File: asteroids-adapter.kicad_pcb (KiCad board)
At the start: 2 copper layers, 88 x 90.2 mm, 15 parts, among them J1 Asteroids PCB connector, J2 Asteroids harness connector, U1 TL074

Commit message: Fixed DC-DC footprint and silk screen info
- Downloaded from CUI website

- fixed connector labels
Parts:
- VR1: value CUI PESE1-S5-D15-M 5V to +/-15V DC-DC converter 34 mA -> CUI PESE1-S5-D15-M; footprint asteroids-adapter:CUI PESE1 DC-DC dual out -> asteroids-adapter:CONV_PESE1-S5-D15-M
- moved C1 2.19 mm to (170.5, 99.8)
- moved VR1 1.32 mm to (167.8, 108.3), turned to 90 degrees
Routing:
- net +15V: track 35.4 -> 37.5 mm
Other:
- board text added: "(Harness)"
- board text added: "(PCB)"
- board text added: "1"
- board text added: "22"
- board text added: "J1"
- board text added: "J2"
- board text removed: "Harness"
- board text removed: "PCB"

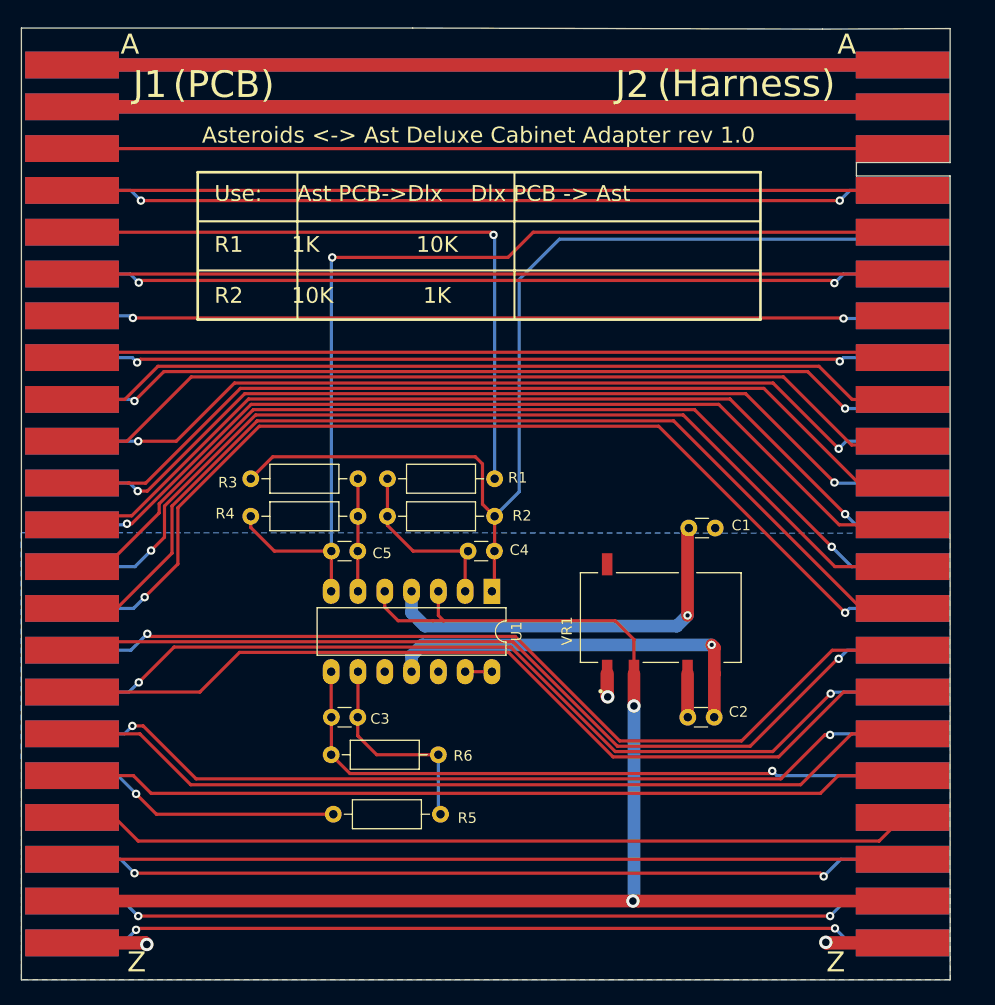
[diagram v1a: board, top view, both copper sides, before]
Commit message: Make sure all the caps have library symbols
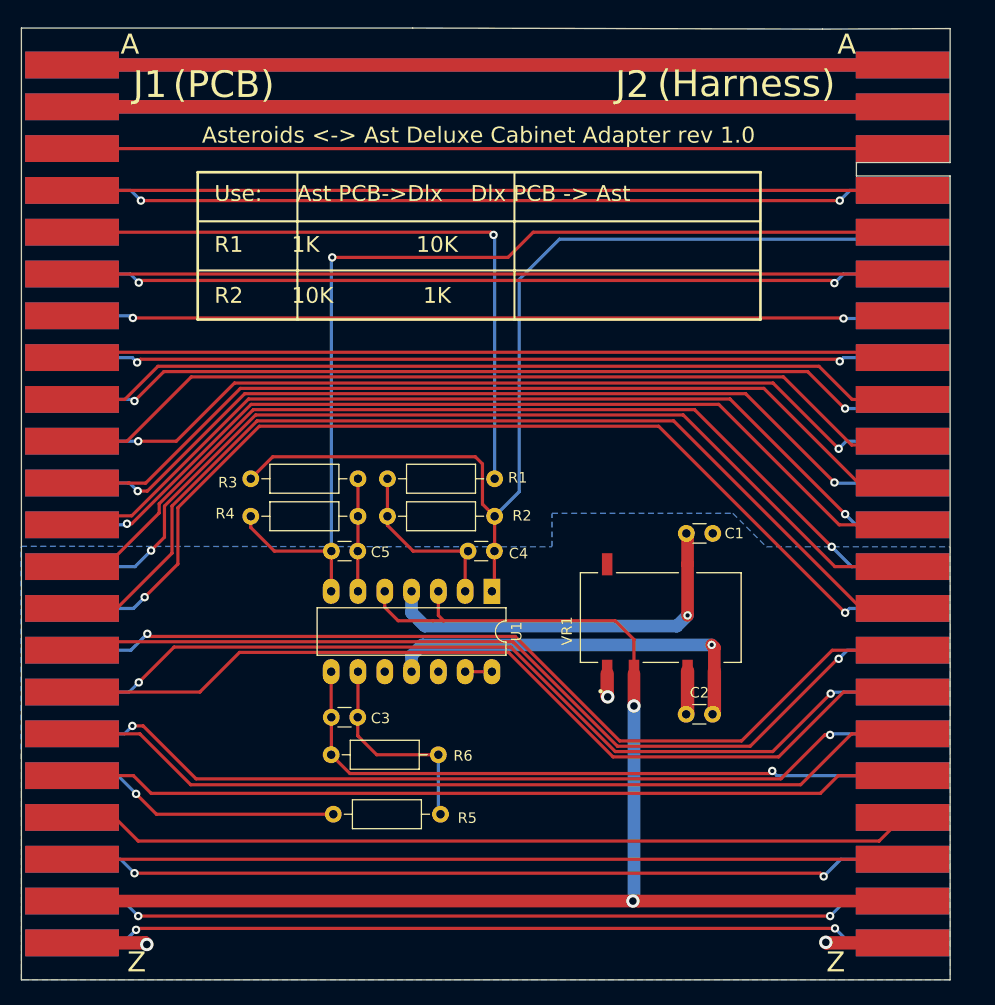
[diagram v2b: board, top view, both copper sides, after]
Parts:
- C1, C2: value Kemet MLCC 100 pF 5% 25V TH -> Kemet 10 uF 25V MLCC TH
- moved C1 2.32 mm to (172.7, 100.3), turned to 180 degrees
- moved C2 0.32 mm to (170.2, 117.5)
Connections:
- C1 pad 1: +15V -> GND
- C1 pad 2: GND -> +15V
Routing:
- net +15V: track 37.5 -> 37.0 mm

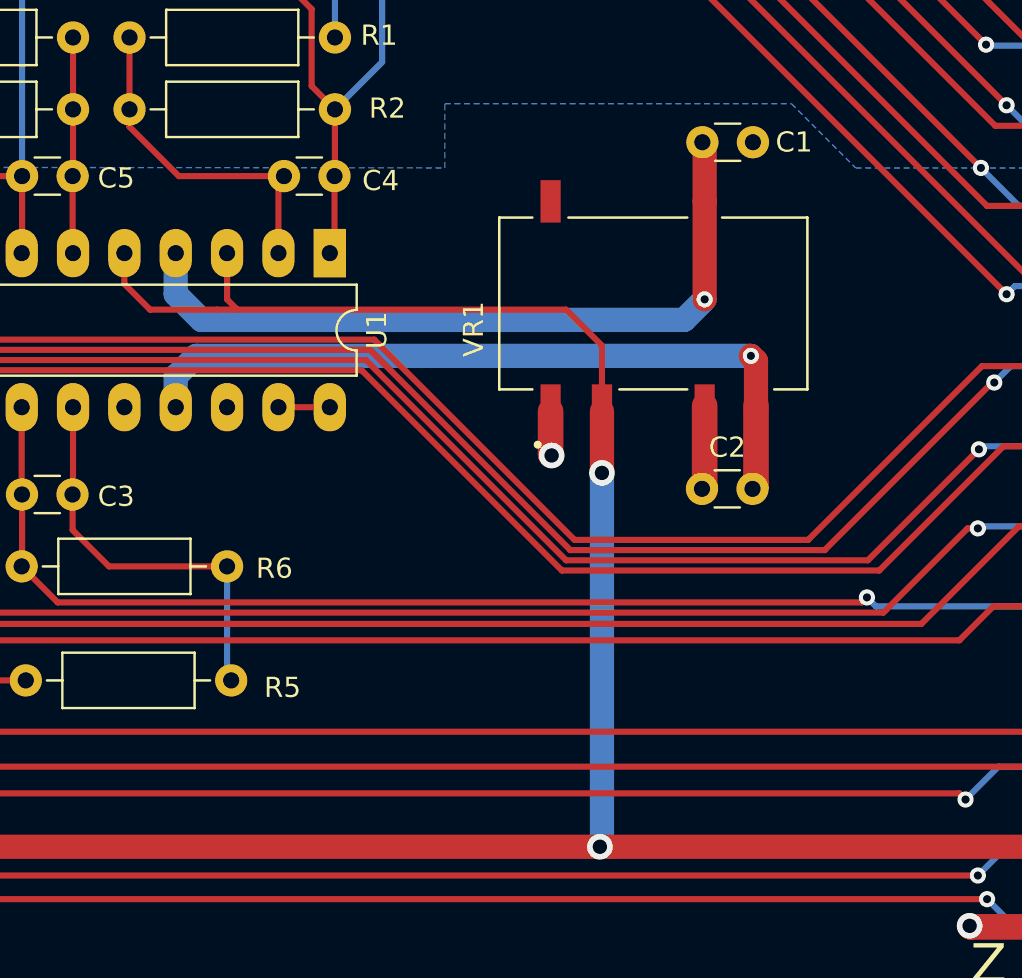
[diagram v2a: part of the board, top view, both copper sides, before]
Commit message: Replace SMT DC/DC converter with Through-hole Part
Retro hobbyists prefer through hole.
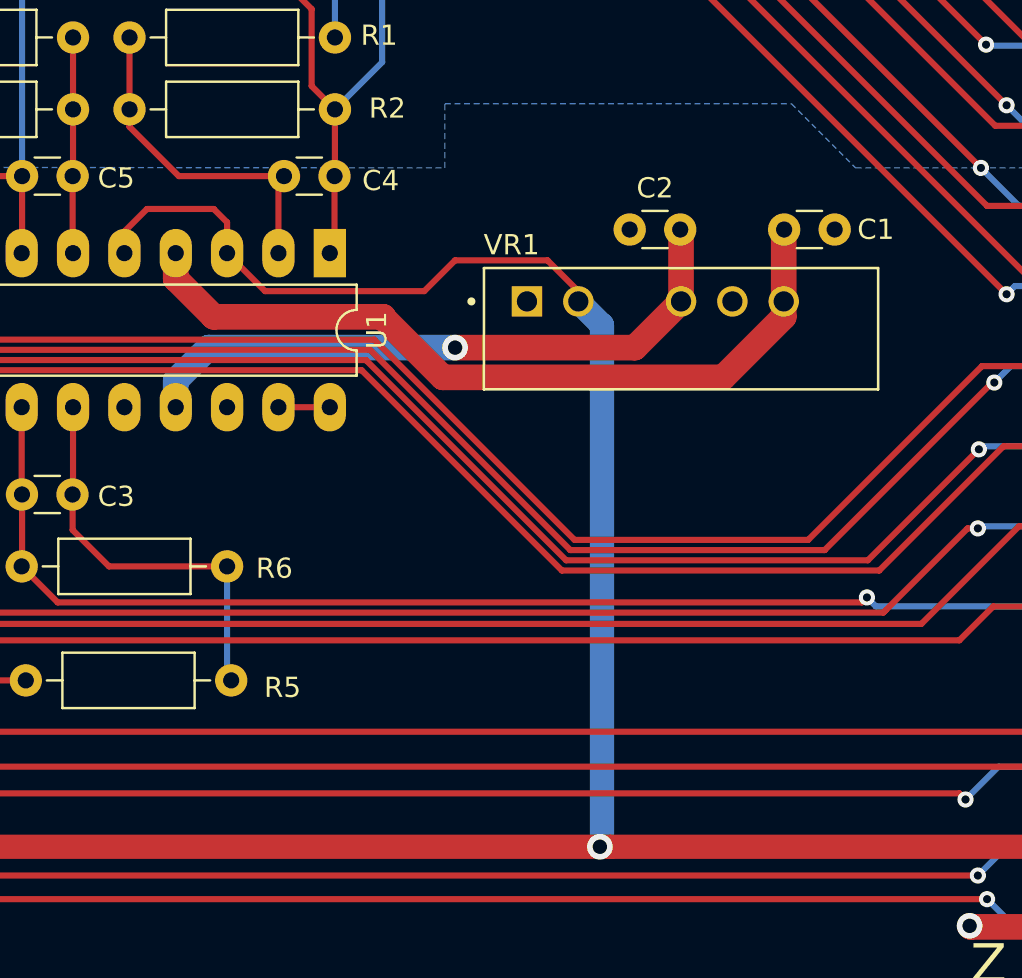
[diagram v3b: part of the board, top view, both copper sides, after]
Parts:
- VR1: value CUI PESE1-S5-D15-M -> CUI PDM1-S5-D15-S; footprint asteroids-adapter:CONV_PESE1-S5-D15-M -> asteroids-adapter:CONV_PDM1-S5-D15-S
- moved C2 13.3 mm to (166.6, 104.6)
- moved VR1 6.25 mm to (161.5, 108.2), turned to 0 degrees
- moved C1 5.92 mm to (176.8, 104.6)
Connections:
- VR1 pad 4: GND -> -15V
- VR1 pad 5: -15V -> GND
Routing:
- net GND: track 20.9 -> 14.5 mm, vias 3 -> 2
- net -15V: track 37.4 -> 31.5 mm
- net +15V: track 37.0 -> 39.0 mm, vias 1 -> 0
- net +5V: track 133.0 -> 134.6 mm, vias 2 -> 1

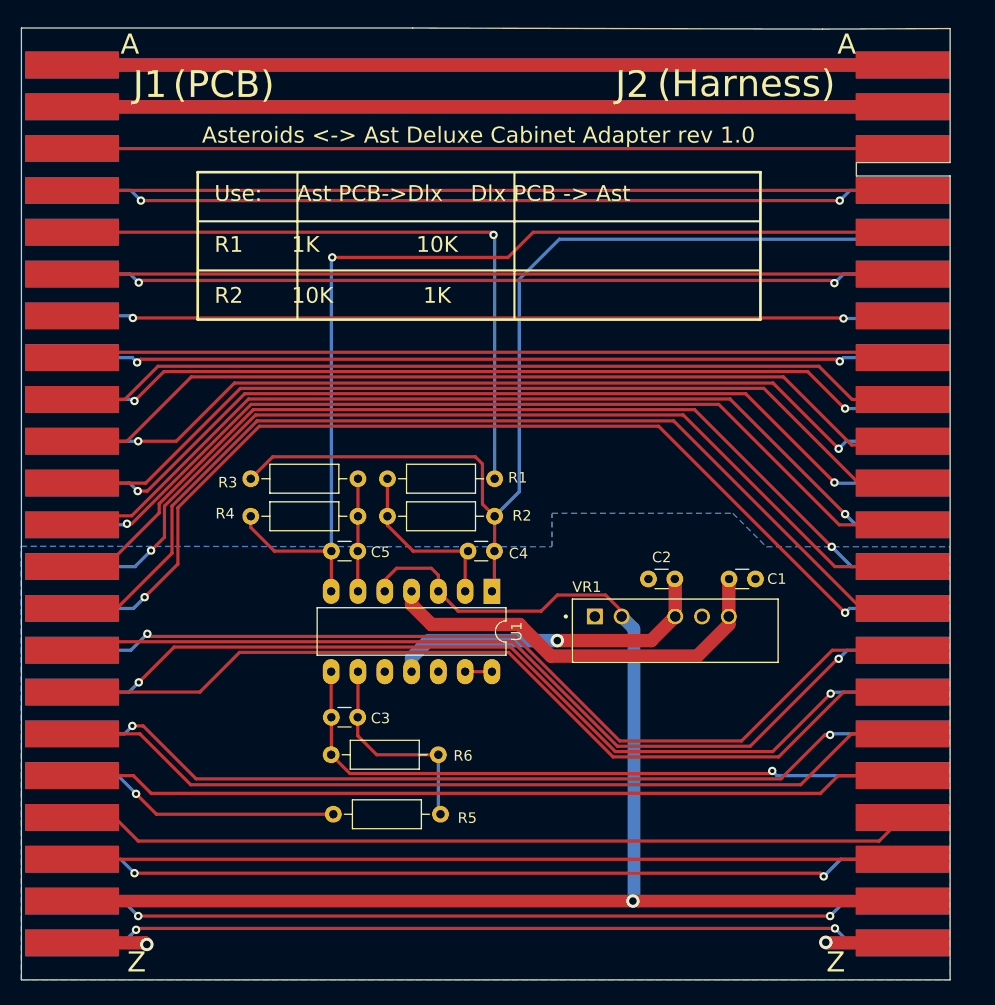
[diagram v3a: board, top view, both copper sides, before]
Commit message: No solder mask around the edge connectors.
- Original footprint had wrong solder mask layer for bottom layer pads.
Fixed, and also place solder mask keepout over entire length of the
edge connectors

- Trimmed ground pour to prevent "fingers" extending between edge
connector pads.
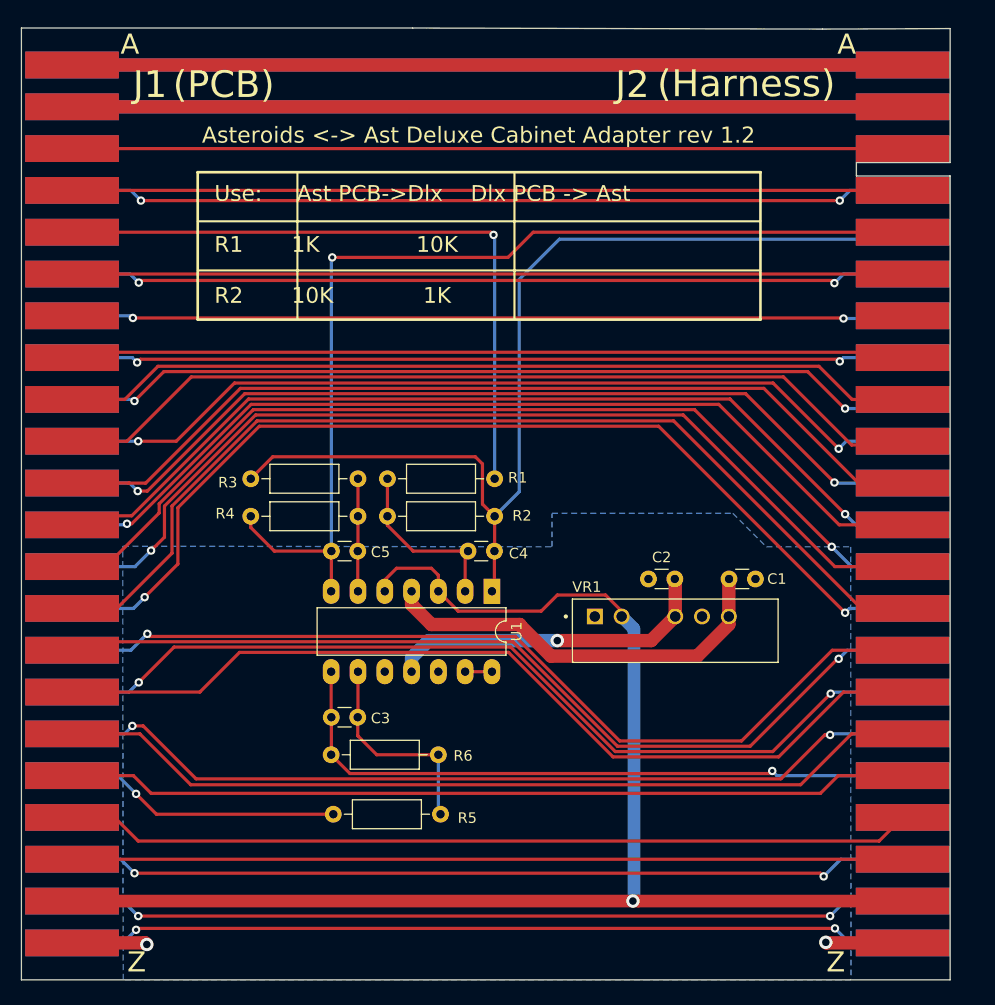
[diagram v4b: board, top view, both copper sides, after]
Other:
- board text added: "Asteroids <-> Ast Deluxe Cabinet Adapter rev 1.2"
- board text removed: "Asteroids <-> Ast Deluxe Cabinet Adapter rev 1.0"

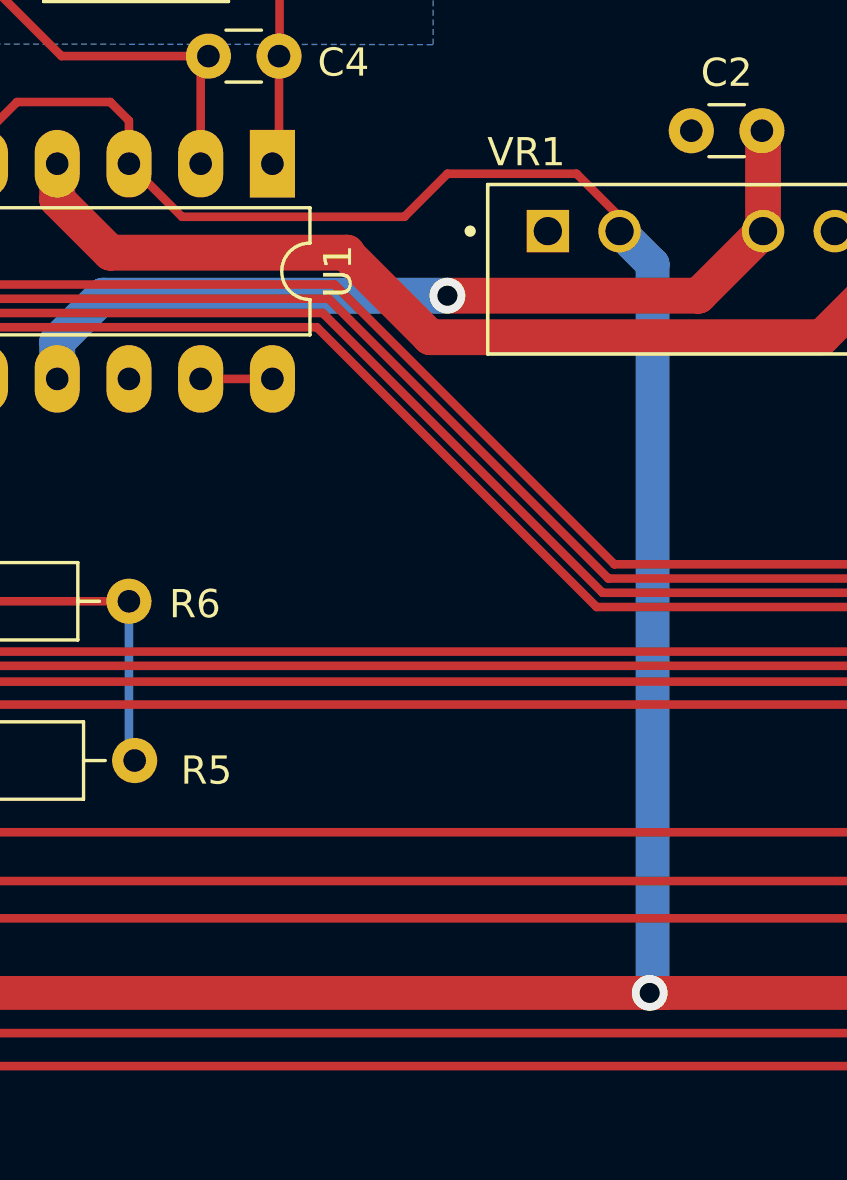
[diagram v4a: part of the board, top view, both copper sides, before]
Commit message: Power and GND to DC-DC converter were swapped
Fixed by swapping the power and ground connections to pins 1 and 2 of
the DC-DC converter.
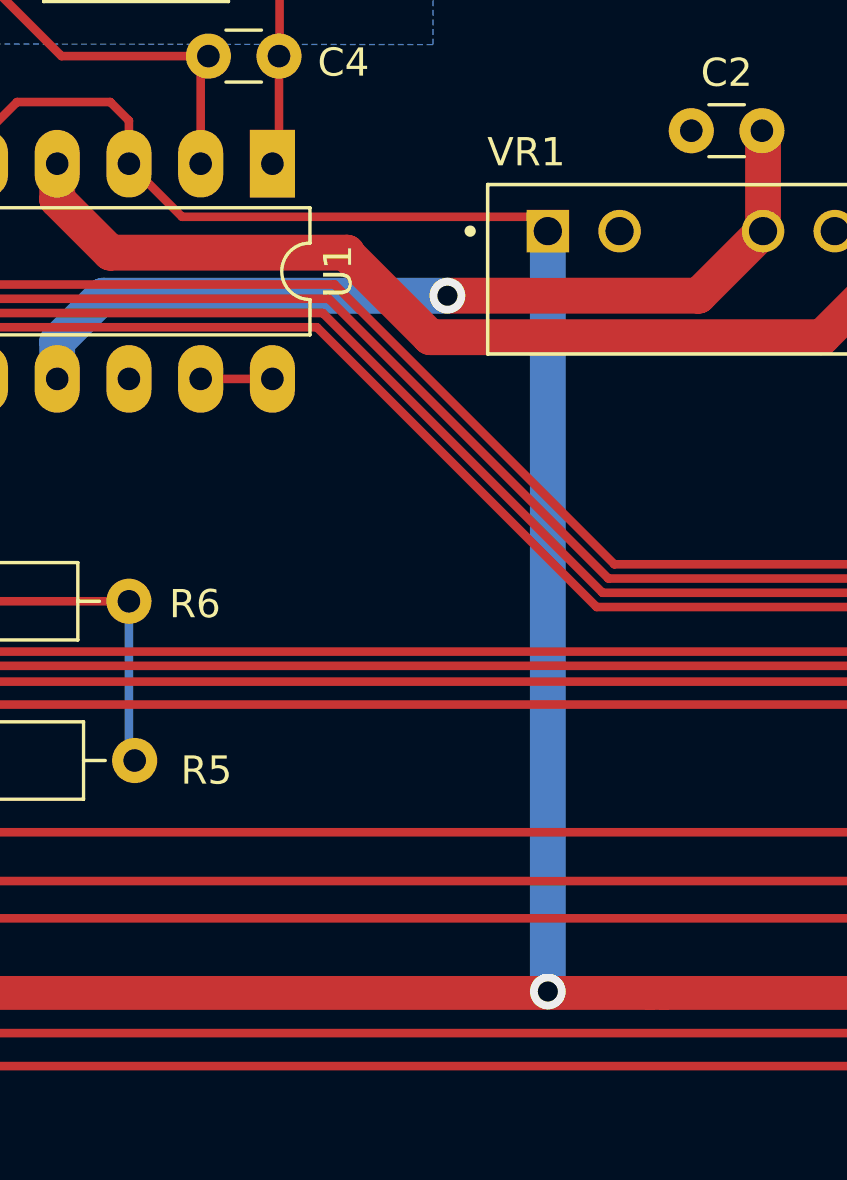
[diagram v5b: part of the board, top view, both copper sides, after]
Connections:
- VR1 pad 1: GND -> +5V
- VR1 pad 2: +5V -> GND
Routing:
- net +5V: track 134.6 -> 129.9 mm
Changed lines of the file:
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@@
     (fp_circle (center -2.75 0) (end -2.65 0) (layer "F.Fab") (width 0.2) (fill none))
     (pad "1" thru_hole rect (at 0 0) (size 1.508 1.508) (drill 1) (layers *.Cu *.Mask)
-      (net 2 "GND") (pinfunction "Vin") (pintype "power_in"))
+      (net 8 "+5V") (pinfunction "Vin") (pintype "power_in"))
     (pad "2" thru_hole circle (at 2.54 0) (size 1.508 1.508) (drill 1) (layers *.Cu *.Mask)
-      (net 8 "+5V") (pinfunction "GND") (pintype "power_in"))
+      (net 2 "GND") (pinfunction "GND") (pintype "power_in"))
     (pad "4" thru_hole circle (at 7.62 0) (size 1.508 1.508) (drill 1) (layers *.Cu *.Mask)
       (net 6 "-15V") (pinfunction "-Vout") (pintype "power_out"))
@@
   (segment (start 141.6304 105.8164) (end 141.6304 104.7496) (width 0.3048) (layer "F.Cu") (net 8))
   (segment (start 165.1508 135.1788) (end 165.6588 135.1788) (width 1.2) (layer "F.Cu") (net 8))
-  (segment (start 164.084 107.696) (end 164.084 108.204) (width 0.3048) (layer "F.Cu") (net 8))
+  (segment (start 146.7104 105.8164) (end 148.59 107.696) (width 0.3048) (layer "F.Cu") (net 8))
   (segment (start 165.6588 135.1788) (end 190.7286 135.1788) (width 1.2) (layer "F.Cu") (net 8))
-  (segment (start 148.59 107.696) (end 156.464 107.696) (width 0.3048) (layer "F.Cu") (net 8))
   (segment (start 146.7104 104.2924) (end 146.7104 105.8164) (width 0.3048) (layer "F.Cu") (net 8))
-  (segment (start 157.988 106.172) (end 162.56 106.172) (width 0.3048) (layer "F.Cu") (net 8))
-  (segment (start 162.56 106.172) (end 164.084 107.696) (width 0.3048) (layer "F.Cu") (net 8))
+  (segment (start 161.036 107.696) (end 161.544 108.204) (width 0.3048) (layer "F.Cu") (net 8))
+  (segment (start 148.59 107.696) (end 161.036 107.696) (width 0.3048) (layer "F.Cu") (net 8))
   (segment (start 146.05 103.632) (end 146.7104 104.2924) (width 0.3048) (layer "F.Cu") (net 8))
   (segment (start 141.6304 104.7496) (end 142.748 103.632) (width 0.3048) (layer "F.Cu") (net 8))
-  (segment (start 146.7104 105.8164) (end 148.59 107.696) (width 0.3048) (layer "F.Cu") (net 8))
   (segment (start 142.748 103.632) (end 146.05 103.632) (width 0.3048) (layer "F.Cu") (net 8))
-  (segment (start 156.464 107.696) (end 157.988 106.172) (width 0.3048) (layer "F.Cu") (net 8))
-  (via (at 165.1508 135.1788) (size 1.27) (drill 0.7112) (layers "F.Cu" "B.Cu") (net 8))
-  (segment (start 164.084 108.204) (end 165.2524 109.3724) (width 1.2) (layer "B.Cu") (net 8))
-  (segment (start 165.2524 109.3724) (end 165.2524 135.0772) (width 1.2) (layer "B.Cu") (net 8))
-  (segment (start 165.2524 135.0772) (end 165.1508 135.1788) (width 1.2) (layer "B.Cu") (net 8))
+  (via (at 161.544 135.128) (size 1.27) (drill 0.7112) (layers "F.Cu" "B.Cu") (net 8))
+  (segment (start 161.544 135.128) (end 161.544 108.204) (width 1.27) (layer "B.Cu") (net 8))
   (segment (start 184.7596 68.7832) (end 118.5164 68.7832) (width 0.3048) (layer "F.Cu") (net 9))
   (via (at 184.7596 68.7832) (size 0.8) (drill 0.4) (layers "F.Cu" "B.Cu") (net 9))
